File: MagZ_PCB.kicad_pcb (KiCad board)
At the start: 4 copper layers, 42 x 42 mm, 13 parts, among them J6 MTQZ, J8 PQ9-Connector

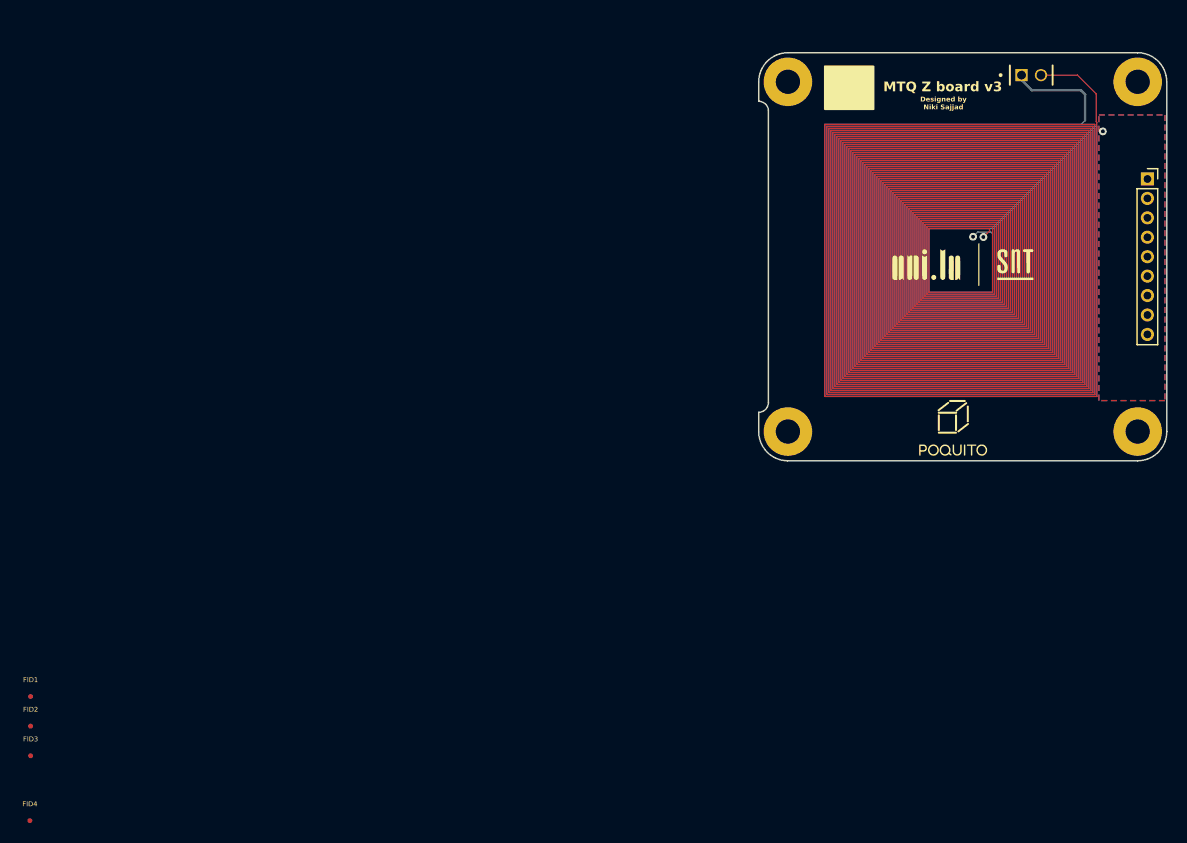
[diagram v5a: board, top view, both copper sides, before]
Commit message: Add cutout for panel L
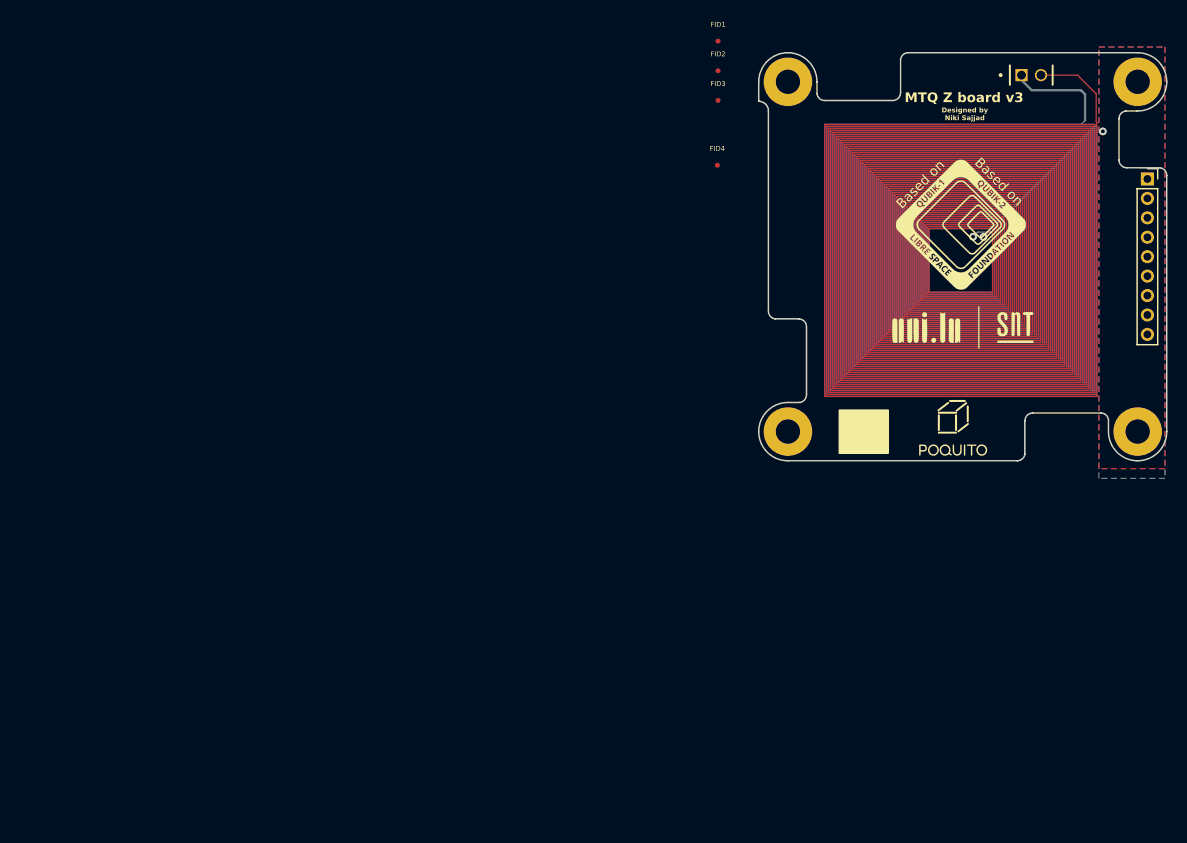
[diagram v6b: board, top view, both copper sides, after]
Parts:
- added REF**: QUBIK-Logo-13x13, lsf-kicad-lib:QUBIK-Logo-13x13, F.Cu at (194.0, 66.3)
- moved FID1 97.8 mm to (169.0, 47.4)
- moved FID2 97.8 mm to (169.0, 50.5)
- moved FID3 97.8 mm to (169.0, 53.5)
- moved FID4 97.8 mm to (168.9, 60.2)
- moved G*** 6.47 mm to (194.6, 76.7)
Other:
- outline, holes or cut-outs redrawn
- board text added: "Based on"
- board text added: "Opening for inductor (mm): 6.0 x 6.0 ± 0.3 Height: 4.2 ± 0.3"
- board text added: "^ solder here"

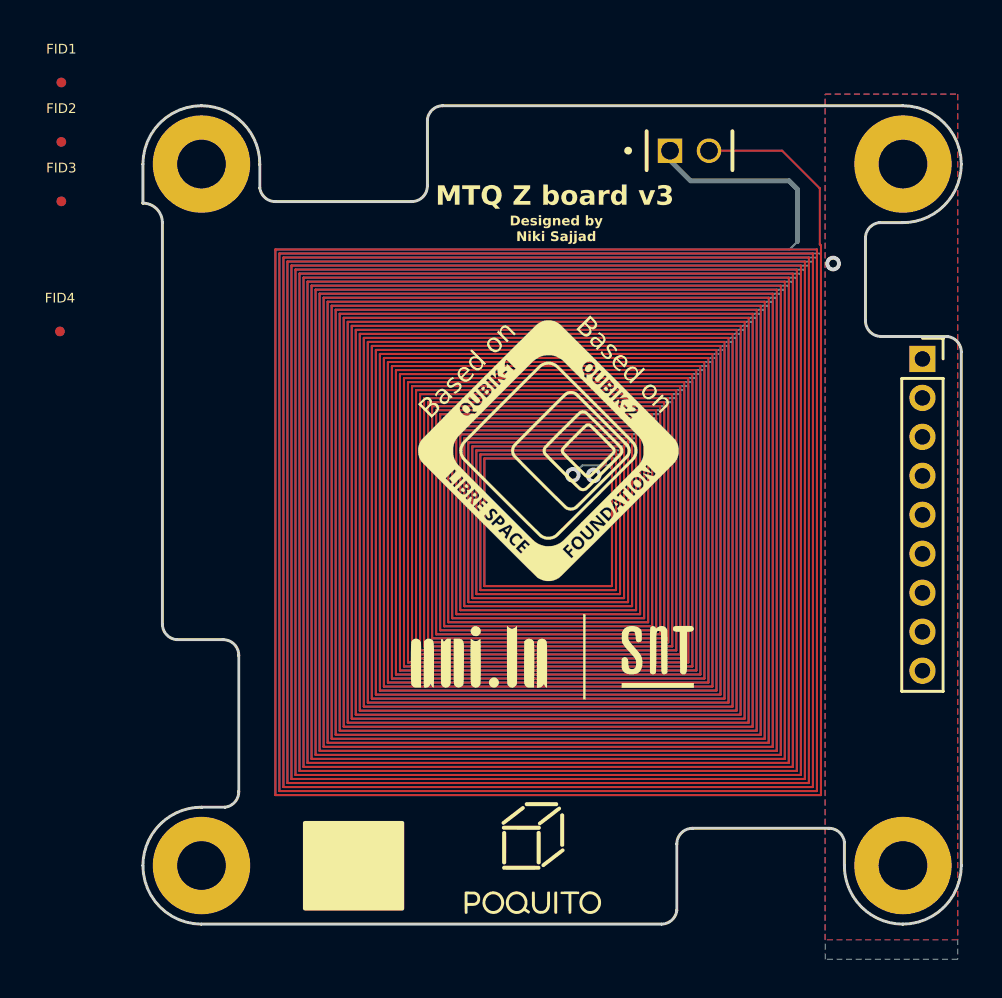
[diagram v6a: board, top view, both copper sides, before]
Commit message: Fix outline DRC
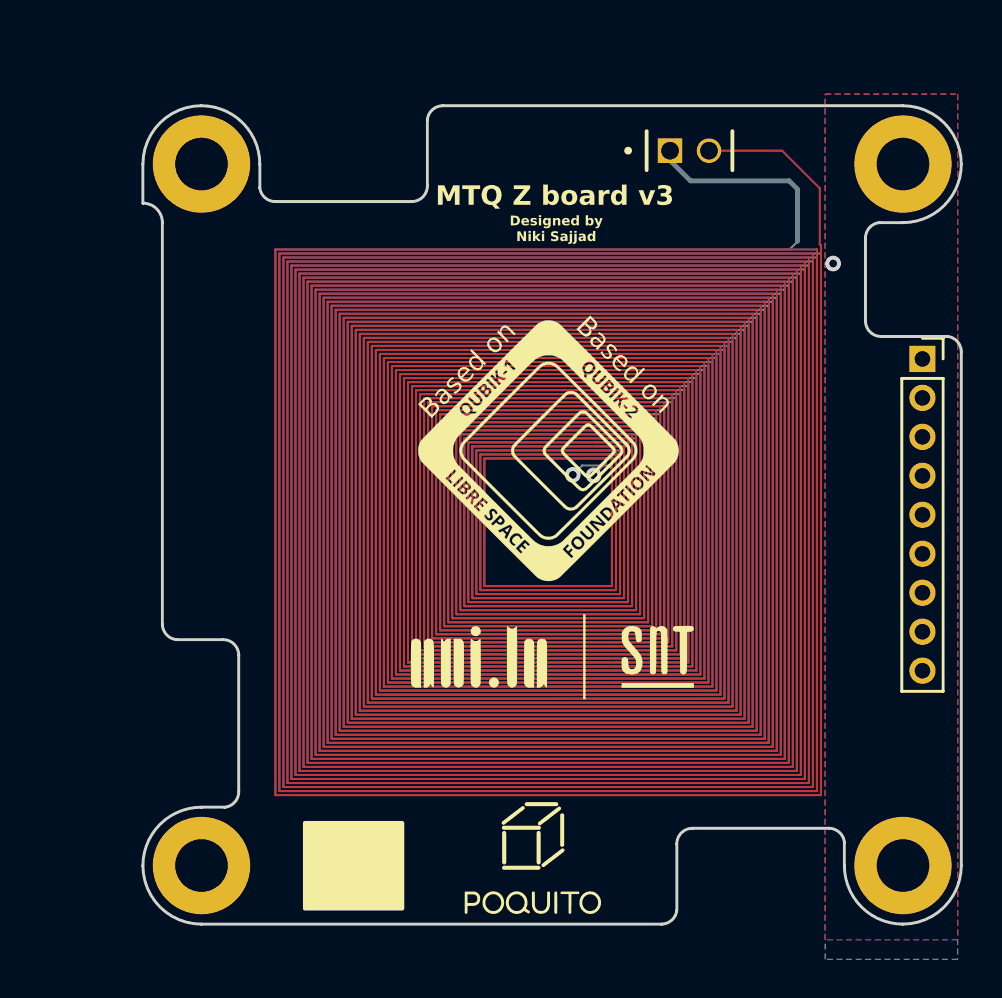
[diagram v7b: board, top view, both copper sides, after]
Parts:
- removed FID1, FID2, FID3, FID4: Fiducial, Fiducial:Fiducial_0.5mm_Mask1.5mm
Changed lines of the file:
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@@
     )
   )
-  (footprint "Fiducial:Fiducial_0.5mm_Mask1.5mm" (layer "F.Cu")
-    (at 168.9282 60.177)
-    (descr "Circular Fiducial, 0.5mm bare copper, 1.5mm soldermask opening")
-    (tags "fiducial")
-    (property "Sheetfile" "NEW_PCB_ADCS.kicad_sch")
-    (property "Sheetname" "")
-    (property "exclude_from_bom" "")
-    (property "ki_description" "Fiducial Marker")
-    (property "ki_keywords" "fiducial marker")
-    (attr smd exclude_from_bom)
-    (fp_text reference "FID4" (at 0 -1.7145 unlocked) (layer "F.SilkS")
-        (effects (font (size 0.5 0.5) (thickness 0.1)))
-    )
-    (fp_text value "Fiducial" (at 0 1.7145 unlocked) (layer "F.Fab")
-        (effects (font (size 0.5 0.5) (thickness 0.1)))
-    )
-    (fp_text user "${REFERENCE}" (at 0 0 unlocked) (layer "F.Fab")
-        (effects (font (size 0.5 0.5) (thickness 0.1)))
-    )
-    (fp_circle (center 0 0) (end 1 0)
-      (stroke (width 0.05) (type solid)) (fill none) (layer "F.CrtYd"))
-    (fp_circle (center 0 0) (end 0.75 0)
-      (stroke (width 0.1) (type solid)) (fill none) (layer "F.Fab"))
-    (pad "" smd circle (at 0 0) (size 0.5 0.5) (layers "F.Cu" "F.Mask")
-      (solder_mask_margin 0.5) (clearance 0.5))
-  )
   (footprint "lsf-kicad-lib:QUBIK-Logo-13x13" (layer "F.Cu")
     (at 194 66.3)
@@
       (stroke (width 0.01) (type solid)) (fill solid) (layer "F.SilkS"))
   )
-  (footprint "Fiducial:Fiducial_0.5mm_Mask1.5mm" (layer "F.Cu")
-    (at 169 50.45)
-    (descr "Circular Fiducial, 0.5mm bare copper, 1.5mm soldermask opening")
-    (tags "fiducial")
-    (property "Sheetfile" "NEW_PCB_ADCS.kicad_sch")
-    (property "Sheetname" "")
-    (property "exclude_from_bom" "")
-    (property "ki_description" "Fiducial Marker")
-    (property "ki_keywords" "fiducial marker")
-    (attr smd exclude_from_bom)
-    (fp_text reference "FID2" (at 0 -1.7145 unlocked) (layer "F.SilkS")
-        (effects (font (size 0.5 0.5) (thickness 0.1)))
-    )
-    (fp_text value "Fiducial" (at 0 1.7145 unlocked) (layer "F.Fab")
-        (effects (font (size 0.5 0.5) (thickness 0.1)))
-    )
-    (fp_text user "${REFERENCE}" (at 0 0 unlocked) (layer "F.Fab")
-        (effects (font (size 0.5 0.5) (thickness 0.1)))
-    )
-    (fp_circle (center 0 0) (end 1 0)
-      (stroke (width 0.05) (type solid)) (fill none) (layer "F.CrtYd"))
-    (fp_circle (center 0 0) (end 0.75 0)
-      (stroke (width 0.1) (type solid)) (fill none) (layer "F.Fab"))
-    (pad "" smd circle (at 0 0) (size 0.5 0.5) (layers "F.Cu" "F.Mask")
-      (solder_mask_margin 0.5) (clearance 0.5))
-  )
-  (footprint "Fiducial:Fiducial_0.5mm_Mask1.5mm" (layer "F.Cu")
-    (at 169 47.4)
-    (descr "Circular Fiducial, 0.5mm bare copper, 1.5mm soldermask opening")
-    (tags "fiducial")
-    (property "Sheetfile" "NEW_PCB_ADCS.kicad_sch")
-    (property "Sheetname" "")
-    (property "exclude_from_bom" "")
-    (property "ki_description" "Fiducial Marker")
-    (property "ki_keywords" "fiducial marker")
-    (attr smd exclude_from_bom)
-    (fp_text reference "FID1" (at 0 -1.7145 unlocked) (layer "F.SilkS")
-        (effects (font (size 0.5 0.5) (thickness 0.1)))
-    )
-    (fp_text value "Fiducial" (at 0 1.7145 unlocked) (layer "F.Fab")
-        (effects (font (size 0.5 0.5) (thickness 0.1)))
-    )
-    (fp_text user "${REFERENCE}" (at 0 0 unlocked) (layer "F.Fab")
-        (effects (font (size 0.5 0.5) (thickness 0.1)))
-    )
-    (fp_circle (center 0 0) (end 1 0)
-      (stroke (width 0.05) (type solid)) (fill none) (layer "F.CrtYd"))
-    (fp_circle (center 0 0) (end 0.75 0)
-      (stroke (width 0.1) (type solid)) (fill none) (layer "F.Fab"))
-    (pad "" smd circle (at 0 0) (size 0.5 0.5) (layers "F.Cu" "F.Mask")
-      (solder_mask_margin 0.5) (clearance 0.5))
-  )
   (footprint "" (layer "F.Cu")
     (at 212.194 87.5879)
@@
         (effects (font (size 1.27 1.27) (thickness 0.15)))
     )
-    (pad "1" thru_hole circle (at 0 0) (size 5 5) (drill 2.5) (layers "*.Cu" "*.Mask")
+    (pad "1" thru_hole circle (at 0 0) (size 5 5) (drill 2.7) (layers "*.Cu" "*.Mask")
       (pinfunction "1") (pintype "input+no_connect"))
   )
-  (footprint "Fiducial:Fiducial_0.5mm_Mask1.5mm" (layer "F.Cu")
-    (at 169 53.5)
-    (descr "Circular Fiducial, 0.5mm bare copper, 1.5mm soldermask opening")
-    (tags "fiducial")
-    (property "Sheetfile" "NEW_PCB_ADCS.kicad_sch")
-    (property "Sheetname" "")
-    (property "exclude_from_bom" "")
-    (property "ki_description" "Fiducial Marker")
-    (property "ki_keywords" "fiducial marker")
-    (attr smd exclude_from_bom)
-    (fp_text reference "FID3" (at 0 -1.7145 unlocked) (layer "F.SilkS")
-        (effects (font (size 0.5 0.5) (thickness 0.1)))
-    )
-    (fp_text value "Fiducial" (at 0 1.7145 unlocked) (layer "F.Fab")
-        (effects (font (size 0.5 0.5) (thickness 0.1)))
-    )
-    (fp_text user "${REFERENCE}" (at 0 0 unlocked) (layer "F.Fab")
-        (effects (font (size 0.5 0.5) (thickness 0.1)))
-    )
-    (fp_circle (center 0 0) (end 1 0)
-      (stroke (width 0.05) (type solid)) (fill none) (layer "F.CrtYd"))
-    (fp_circle (center 0 0) (end 0.75 0)
-      (stroke (width 0.1) (type solid)) (fill none) (layer "F.Fab"))
-    (pad "" smd circle (at 0 0) (size 0.5 0.5) (layers "F.Cu" "F.Mask")
-      (solder_mask_margin 0.5) (clearance 0.5))
-  )
   (footprint "SQT-102-03-F-S:SAMTEC_SQT-102-03-F-S" (layer "F.Cu")
     (at 200.2395 50.9)
@@
         (effects (font (size 1.27 1.27) (thickness 0.15)))
     )
-    (pad "1" thru_hole circle (at 0 0) (size 5 5) (drill 2.5) (layers "*.Cu" "*.Mask")
+    (pad "1" thru_hole circle (at 0 0) (size 5 5) (drill 2.7) (layers "*.Cu" "*.Mask")
       (pinfunction "1") (pintype "input+no_connect"))
   )
@@
         (effects (font (size 1.27 1.27) (thickness 0.15)))
     )
-    (pad "1" thru_hole circle (at 0 0) (size 5 5) (drill 2.5) (layers "*.Cu" "*.Mask")
+    (pad "1" thru_hole circle (at 0 0) (size 5 5) (drill 2.7) (layers "*.Cu" "*.Mask")
       (pinfunction "1") (pintype "input+no_connect"))
   )
@@
         (effects (font (size 1.27 1.27) (thickness 0.15)))
     )
-    (pad "1" thru_hole circle (at 0 0) (size 5 5) (drill 2.5) (layers "*.Cu" "*.Mask")
+    (pad "1" thru_hole circle (at 0 0) (size 5 5) (drill 2.7) (layers "*.Cu" "*.Mask")
       (pinfunction "1") (pintype "input+no_connect"))
   )
@@
   (gr_line (start 179.9814 53.513225) (end 186.9814 53.513225)
     (stroke (width 0.15) (type default)) (layer "Edge.Cuts"))
-  (gr_arc (start 174.9 75.993775) (mid 174.39792 75.736516) (end 174.1872 75.213197)
+  (gr_arc (start 174.9 75.993775) (mid 174.39796 75.736622) (end 174.1872 75.213409)
     (stroke (width 0.15) (type default)) (layer "Edge.Cuts"))
   (gr_line (start 178.106225 83.8) (end 178.106225 76.8)
@@
   (gr_line (start 208.393 85.675175) (end 201.393 85.675175)
     (stroke (width 0.15) (type default)) (layer "Edge.Cuts"))
-  (gr_line (start 214.49792 60.442741) (end 211.0744 60.436138)
+  (gr_line (start 214.49792 60.436138) (end 211.0744 60.436138)
     (stroke (width 0.15) (type default)) (layer "Edge.Cuts"))
   (gr_line (start 179.187173 51.607025) (end 179.187173 52.807)
@@
   (gr_line (start 176.1872 90.5942) (end 199.806197 90.5942)
     (stroke (width 0.15) (type default)) (layer "Edge.Cuts"))
-  (gr_arc (start 214.49792 60.442741) (mid 214.988038 60.704155) (end 215.1872 61.2227)
+  (gr_arc (start 214.49792 60.436138) (mid 214.989386 60.701163) (end 215.1872 61.223319)
     (stroke (width 0.15) (type default)) (layer "Edge.Cuts"))
   (gr_line (start 174.1872 54.5942) (end 174.1872 75.213409)
@@
   (gr_line (start 174.9 75.993775) (end 177.3 75.993775)
     (stroke (width 0.15) (type default)) (layer "Edge.Cuts"))
-  (gr_arc (start 173.1872 53.5942) (mid 173.89369 53.886477) (end 174.187198 54.592455)
+  (gr_arc (start 173.1872 53.5942) (mid 173.89405 53.887349) (end 174.187198 54.5942)
     (stroke (width 0.15) (type solid)) (layer "Edge.Cuts"))
   (gr_arc (start 178.106225 83.8) (mid 177.903318 84.330675) (end 177.4 84.594227)
